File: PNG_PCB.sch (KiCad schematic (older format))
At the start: 1 part, among them U1 Teensy4.1

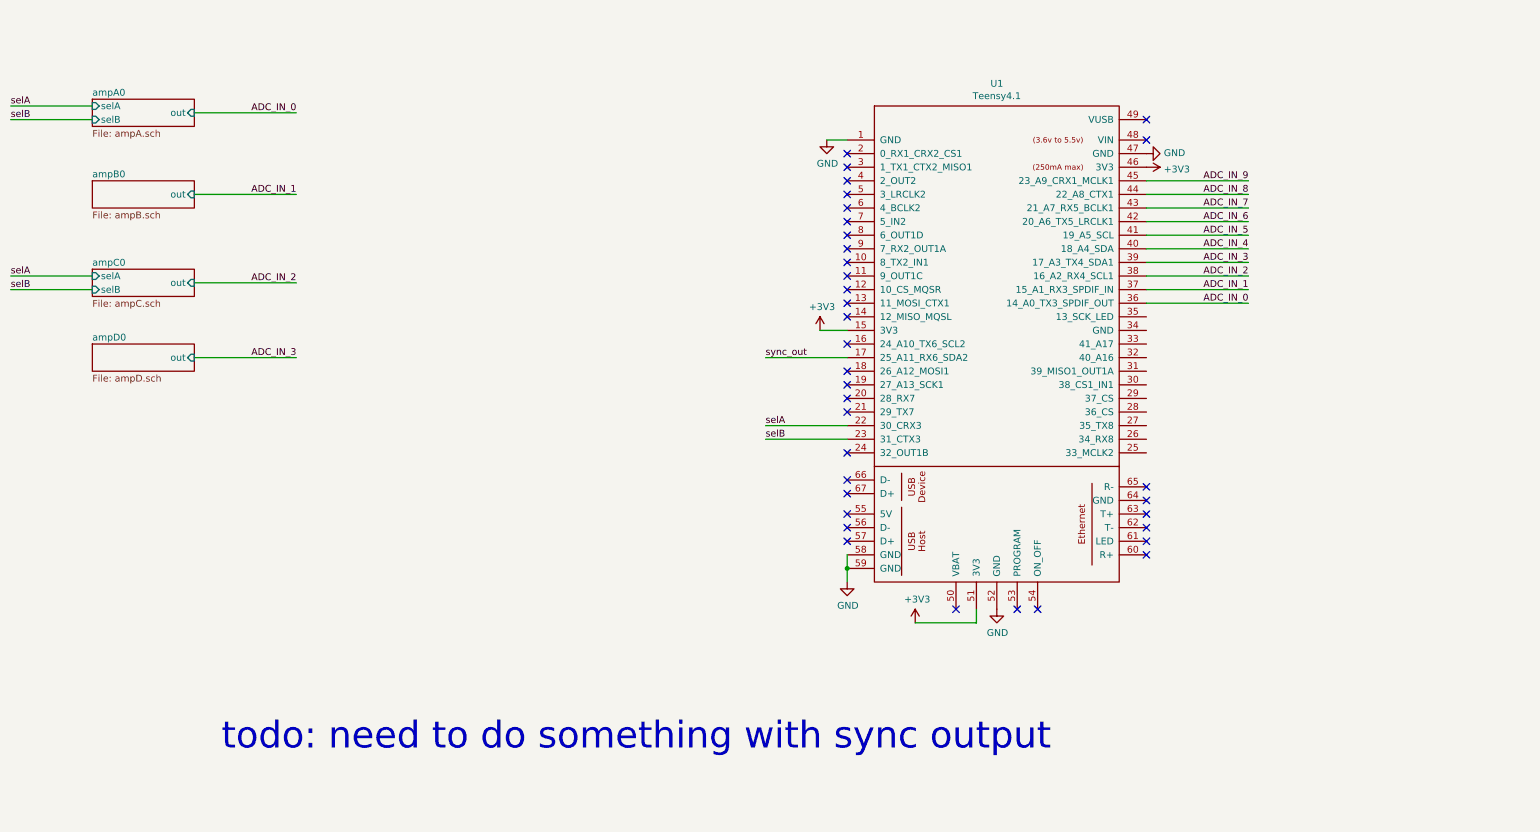
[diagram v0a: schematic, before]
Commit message: added all adc outputs
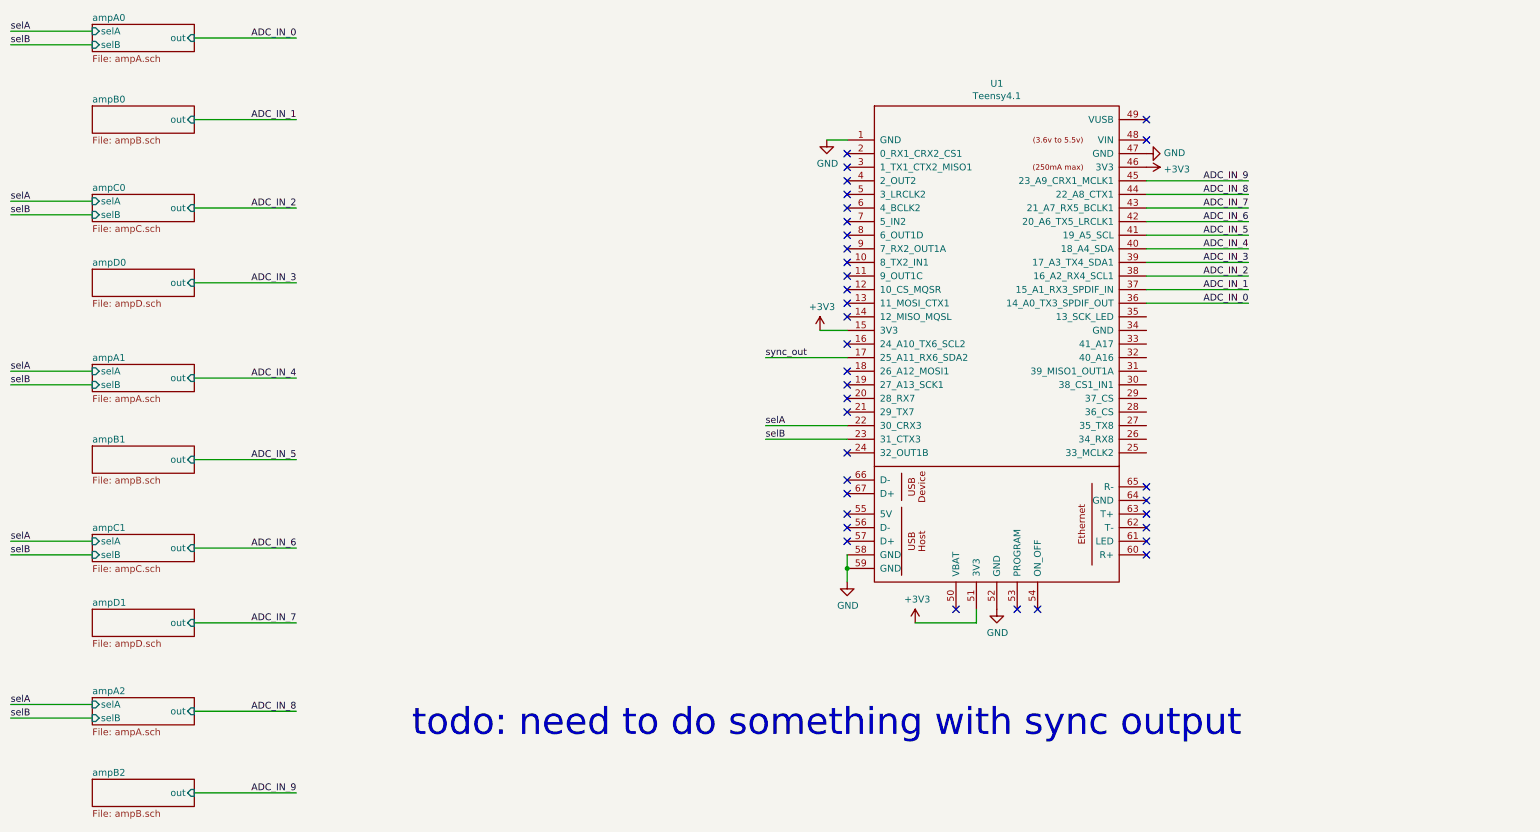
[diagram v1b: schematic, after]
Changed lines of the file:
@@
 $Descr A4 11693 8268
 encoding utf-8
-Sheet 1 5
+Sheet 1 11
 Title ""
 Date ""
@@
 ADC_IN_0
 $Sheet
-S 1750 1350 750  200
+S 1750 800  750  200
 U 6017CC5E
 F0 "ampA0" 50
 F1 "ampA.sch" 50
-F2 "out" I R 2500 1450 50
-F3 "selA" I L 1750 1400 50
-F4 "selB" I L 1750 1500 50
-$EndSheet
-$Sheet
-S 1750 1950 750  200
+F2 "out" I R 2500 900 50
+F3 "selA" I L 1750 850 50
+F4 "selB" I L 1750 950 50
+$EndSheet
+$Sheet
+S 1750 1400 750  200
 U 601927EB
 F0 "ampB0" 50
 F1 "ampB.sch" 50
-F2 "out" I R 2500 2050 50
-$EndSheet
-$Sheet
-S 1750 2600 750  200
+F2 "out" I R 2500 1500 50
+$EndSheet
+$Sheet
+S 1750 2050 750  200
 U 6019C043
 F0 "ampC0" 50
 F1 "ampC.sch" 50
-F2 "out" I R 2500 2700 50
-F3 "selA" I L 1750 2650 50
-F4 "selB" I L 1750 2750 50
-$EndSheet
-$Sheet
-S 1750 3150 750  200
+F2 "out" I R 2500 2150 50
+F3 "selA" I L 1750 2100 50
+F4 "selB" I L 1750 2200 50
+$EndSheet
+$Sheet
+S 1750 2600 750  200
 U 6019DBCE
 F0 "ampD0" 50
 F1 "ampD.sch" 50
-F2 "out" I R 2500 3250 50
-$EndSheet
-$Comp
-L power:GND #PWR?
+F2 "out" I R 2500 2700 50
+$EndSheet
+$Comp
+L power:GND #PWR05
 U 1 1 601A016E
 P 8400 5100
-F 0 "#PWR?" H 8400 4850 50  0001 C CNN
+F 0 "#PWR05" H 8400 4850 50  0001 C CNN
 F 1 "GND" H 8405 4927 50  0000 C CNN
 F 2 "" H 8400 5100 50  0001 C CNN
@@
 $EndComp
 $Comp
-L power:+3V3 #PWR?
+L power:+3V3 #PWR04
 U 1 1 601A19F5
 P 7800 5200
-F 0 "#PWR?" H 7800 5050 50  0001 C CNN
+F 0 "#PWR04" H 7800 5050 50  0001 C CNN
 F 1 "+3V3" H 7815 5373 50  0000 C CNN
 F 2 "" H 7800 5200 50  0001 C CNN
@@
 NoConn ~ 7300 4150
 $Comp
-L power:GND #PWR?
+L power:GND #PWR03
 U 1 1 601A37A3
 P 7300 4900
-F 0 "#PWR?" H 7300 4650 50  0001 C CNN
+F 0 "#PWR03" H 7300 4650 50  0001 C CNN
 F 1 "GND" H 7305 4727 50  0000 C CNN
 F 2 "" H 7300 4900 50  0001 C CNN
@@
 ADC_IN_9
 $Comp
-L power:+3V3 #PWR?
+L power:+3V3 #PWR07
 U 1 1 601A66F3
 P 9500 1850
-F 0 "#PWR?" H 9500 1700 50  0001 C CNN
+F 0 "#PWR07" H 9500 1700 50  0001 C CNN
 F 1 "+3V3" V 9515 1978 50  0000 L CNN
 F 2 "" H 9500 1850 50  0001 C CNN
@@
 $EndComp
 $Comp
-L power:GND #PWR?
+L power:GND #PWR06
 U 1 1 601A740A
 P 9500 1750
-F 0 "#PWR?" H 9500 1500 50  0001 C CNN
+F 0 "#PWR06" H 9500 1500 50  0001 C CNN
 F 1 "GND" V 9505 1622 50  0000 R CNN
 F 2 "" H 9500 1750 50  0001 C CNN
@@
 NoConn ~ 9500 1500
 $Comp
-L power:GND #PWR?
+L power:GND #PWR02
 U 1 1 601A93E9
 P 7150 1650
-F 0 "#PWR?" H 7150 1400 50  0001 C CNN
+F 0 "#PWR02" H 7150 1400 50  0001 C CNN
 F 1 "GND" H 7155 1477 50  0000 C CNN
 F 2 "" H 7150 1650 50  0001 C CNN
@@
 NoConn ~ 7300 3650
 $Comp
-L power:+3V3 #PWR?
+L power:+3V3 #PWR01
 U 1 1 601AD0C3
 P 7100 3050
-F 0 "#PWR?" H 7100 2900 50  0001 C CNN
+F 0 "#PWR01" H 7100 2900 50  0001 C CNN
 F 1 "+3V3" H 7115 3223 50  0000 C CNN
 F 2 "" H 7100 3050 50  0001 C CNN
@@
 Text Label 6700 3250 0    50   ~ 0
 sync_out
-Text Notes 2700 6150 0    197  ~ 0
+Text Notes 4100 6050 0    197  ~ 0
 todo: need to do something with sync output
-Text Label 1150 1400 0    50   ~ 0
-selA
-Text Label 1150 1500 0    50   ~ 0
-selB
-Wire Wire Line
-	1750 1400 1150 1400
-Wire Wire Line
-	1750 1500 1150 1500
-Text Label 1150 2650 0    50   ~ 0
-selA
-Text Label 1150 2750 0    50   ~ 0
-selB
-Wire Wire Line
-	1750 2650 1150 2650
-Wire Wire Line
-	1750 2750 1150 2750
-Wire Wire Line
-	2500 1450 3250 1450
-Text Label 3250 1450 2    50   ~ 0
+Text Label 1150 850  0    50   ~ 0
+selA
+Text Label 1150 950  0    50   ~ 0
+selB
+Wire Wire Line
+	1750 850  1150 850
+Wire Wire Line
+	1750 950  1150 950
+Text Label 1150 2100 0    50   ~ 0
+selA
+Text Label 1150 2200 0    50   ~ 0
+selB
+Wire Wire Line
+	1750 2100 1150 2100
+Wire Wire Line
+	1750 2200 1150 2200
+Wire Wire Line
+	2500 900  3250 900
+Text Label 3250 900  2    50   ~ 0
 ADC_IN_0
 Wire Wire Line
-	2500 2050 3250 2050
-Text Label 3250 2050 2    50   ~ 0
+	2500 1500 3250 1500
+Text Label 3250 1500 2    50   ~ 0
 ADC_IN_1
+Wire Wire Line
+	2500 2150 3250 2150
+Text Label 3250 2150 2    50   ~ 0
+ADC_IN_2
 Wire Wire Line
 	2500 2700 3250 2700
 Text Label 3250 2700 2    50   ~ 0
-ADC_IN_2
-Wire Wire Line
-	2500 3250 3250 3250
-Text Label 3250 3250 2    50   ~ 0
 ADC_IN_3
+$Sheet
+S 1750 3300 750  200
+U 601B4C0E
+F0 "ampA1" 50
+F1 "ampA.sch" 50
+F2 "out" I R 2500 3400 50
+F3 "selA" I L 1750 3350 50
+F4 "selB" I L 1750 3450 50
+$EndSheet
+$Sheet
+S 1750 3900 750  200
+U 601B4C11
+F0 "ampB1" 50
+F1 "ampB.sch" 50
+F2 "out" I R 2500 4000 50
+$EndSheet
+$Sheet
+S 1750 4550 750  200
+U 601B4C16
+F0 "ampC1" 50
+F1 "ampC.sch" 50
+F2 "out" I R 2500 4650 50
+F3 "selA" I L 1750 4600 50
+F4 "selB" I L 1750 4700 50
+$EndSheet
+$Sheet
+S 1750 5100 750  200
+U 601B4C19
+F0 "ampD1" 50
+F1 "ampD.sch" 50
+F2 "out" I R 2500 5200 50
+$EndSheet
+Text Label 1150 3350 0    50   ~ 0
+selA
+Text Label 1150 3450 0    50   ~ 0
+selB
+Wire Wire Line
+	1750 3350 1150 3350
+Wire Wire Line
+	1750 3450 1150 3450
+Text Label 1150 4600 0    50   ~ 0
+selA
+Text Label 1150 4700 0    50   ~ 0
+selB
+Wire Wire Line
+	1750 4600 1150 4600
+Wire Wire Line
+	1750 4700 1150 4700
+Wire Wire Line
+	2500 3400 3250 3400
+Text Label 3250 3400 2    50   ~ 0
+ADC_IN_4
+Wire Wire Line
+	2500 4000 3250 4000
+Text Label 3250 4000 2    50   ~ 0
+ADC_IN_5
+Wire Wire Line
+	2500 4650 3250 4650
+Text Label 3250 4650 2    50   ~ 0
+ADC_IN_6
+Wire Wire Line
+	2500 5200 3250 5200
+Text Label 3250 5200 2    50   ~ 0
+ADC_IN_7
+$Sheet
+S 1750 5750 750  200
+U 601B73B7
+F0 "ampA2" 50
+F1 "ampA.sch" 50
+F2 "out" I R 2500 5850 50
+F3 "selA" I L 1750 5800 50
+F4 "selB" I L 1750 5900 50
+$EndSheet
+$Sheet
+S 1750 6350 750  200
+U 601B73BA
+F0 "ampB2" 50
+F1 "ampB.sch" 50
+F2 "out" I R 2500 6450 50
+$EndSheet
+Text Label 1150 5800 0    50   ~ 0
+selA
+Text Label 1150 5900 0    50   ~ 0
+selB
+Wire Wire Line
+	1750 5800 1150 5800
+Wire Wire Line
+	1750 5900 1150 5900
+Wire Wire Line
+	2500 5850 3250 5850
+Text Label 3250 5850 2    50   ~ 0
+ADC_IN_8
+Wire Wire Line
+	2500 6450 3250 6450
+Text Label 3250 6450 2    50   ~ 0
+ADC_IN_9
 $EndSCHEMATC

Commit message: added screw terminal port for sync output
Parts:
- added U?: screw_term, Connector_PinHeader_1.27mm:PinHeader_1x02_P1.27mm_Vertical, symbol PNG_PCB_Parts:screw_term
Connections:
- net sync_out: now also U?.1 (a)
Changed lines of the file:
@@
 Text Label 3250 6450 2    50   ~ 0
 ADC_IN_9
+Wire Wire Line
+	5000 3250 4400 3250
+Text Label 4400 3250 0    50   ~ 0
+sync_out
+$Comp
+L PNG_PCB_Parts:screw_term U?
+U 1 1 601BAD2F
+P 5000 3250
+F 0 "U?" H 5058 3384 50  0000 L CNN
+F 1 "screw_term" H 5058 3293 50  0000 L CNN
+F 2 "Connector_PinHeader_1.27mm:PinHeader_1x02_P1.27mm_Vertical" H 5000 3250 50  0001 C CNN
+F 3 "" H 5000 3250 50  0001 C CNN
+	1    5000 3250
+	1    0    0    -1
+$EndComp
 $EndSCHEMATC

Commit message: fixed sync output and added sync input
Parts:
- added U?: screw_term, Connector_PinHeader_1.27mm:PinHeader_1x02_P1.27mm_Vertical, symbol PNG_PCB_Parts:screw_term
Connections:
- net sync_out: now also U1.2 (0_RX1_CRX2_CS1), U?.2 (b); no longer U1.17 (25_A11_RX6_SDA2), U?.1 (a)
- new net sync_in: U1.17 (25_A11_RX6_SDA2), U?.1 (a)
- no-connect marks 35 -> 34
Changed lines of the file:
@@
 L power:GND #PWR02
 U 1 1 601A93E9
-P 7150 1650
-F 0 "#PWR02" H 7150 1400 50  0001 C CNN
-F 1 "GND" H 7155 1477 50  0000 C CNN
-F 2 "" H 7150 1650 50  0001 C CNN
-F 3 "" H 7150 1650 50  0001 C CNN
-	1    7150 1650
-	1    0    0    -1
-$EndComp
-Wire Wire Line
-	7300 1650 7150 1650
-NoConn ~ 7300 1750
+P 7300 1650
+F 0 "#PWR02" H 7300 1400 50  0001 C CNN
+F 1 "GND" V 7305 1522 50  0000 R CNN
+F 2 "" H 7300 1650 50  0001 C CNN
+F 3 "" H 7300 1650 50  0001 C CNN
+	1    7300 1650
+	0    1    1    0
+$EndComp
 NoConn ~ 7300 1850
 NoConn ~ 7300 1950
@@
 	7300 3250 6700 3250
 Text Label 6700 3250 0    50   ~ 0
-sync_out
+sync_in
 Text Notes 4100 6050 0    197  ~ 0
 todo: need to do something with sync output
@@
 	5000 3250 4400 3250
 Text Label 4400 3250 0    50   ~ 0
-sync_out
+sync_in
 $Comp
 L PNG_PCB_Parts:screw_term U?
@@
 	1    0    0    -1
 $EndComp
+Wire Wire Line
+	7300 1750 6700 1750
+Text Label 6700 1750 0    50   ~ 0
+sync_out
+Wire Wire Line
+	5000 3600 4400 3600
+Text Label 4400 3600 0    50   ~ 0
+sync_out
+$Comp
+L PNG_PCB_Parts:screw_term U?
+U 2 1 601BD94C
+P 5000 3600
+F 0 "U?" H 5058 3734 50  0000 L CNN
+F 1 "screw_term" H 5058 3643 50  0000 L CNN
+F 2 "Connector_PinHeader_1.27mm:PinHeader_1x02_P1.27mm_Vertical" H 5000 3600 50  0001 C CNN
+F 3 "" H 5000 3600 50  0001 C CNN
+	2    5000 3600
+	1    0    0    -1
+$EndComp

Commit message: annotated sync in and out
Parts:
- gave numbers to parts that had none: 1
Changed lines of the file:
@@
 sync_in
 $Comp
-L PNG_PCB_Parts:screw_term U?
+L PNG_PCB_Parts:screw_term U31
 U 1 1 601BAD2F
 P 5000 3250
-F 0 "U?" H 5058 3384 50  0000 L CNN
+F 0 "U31" H 5058 3384 50  0000 L CNN
 F 1 "screw_term" H 5058 3293 50  0000 L CNN
 F 2 "Connector_PinHeader_1.27mm:PinHeader_1x02_P1.27mm_Vertical" H 5000 3250 50  0001 C CNN
@@
 sync_out
 $Comp
-L PNG_PCB_Parts:screw_term U?
+L PNG_PCB_Parts:screw_term U31
 U 2 1 601BD94C
 P 5000 3600
-F 0 "U?" H 5058 3734 50  0000 L CNN
+F 0 "U31" H 5058 3734 50  0000 L CNN
 F 1 "screw_term" H 5058 3643 50  0000 L CNN
 F 2 "Connector_PinHeader_1.27mm:PinHeader_1x02_P1.27mm_Vertical" H 5000 3600 50  0001 C CNN

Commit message: added no connects on teensy
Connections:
- no-connect marks 34 -> 45
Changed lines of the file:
@@
 	1    0    0    -1
 $EndComp
+NoConn ~ 9500 2950
+NoConn ~ 9500 3050
+NoConn ~ 9500 3150
+NoConn ~ 9500 3250
+NoConn ~ 9500 3350
+NoConn ~ 9500 3450
+NoConn ~ 9500 3550
+NoConn ~ 9500 3650
+NoConn ~ 9500 3750
+NoConn ~ 9500 3850
+NoConn ~ 9500 3950
 $EndSCHEMATC

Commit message: added all muxes to the board
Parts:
- renumbered U31 to U1, U1 to U2
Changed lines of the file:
@@
 $EndDescr
 $Comp
-L teensy:Teensy4.1 U1
+L teensy:Teensy4.1 U2
 U 1 1 60133249
 P 8400 3800
-F 0 "U1" H 8400 6365 50  0000 C CNN
+F 0 "U2" H 8400 6365 50  0000 C CNN
 F 1 "Teensy4.1" H 8400 6274 50  0000 C CNN
 F 2 "teensy:Teensy41" H 8000 4200 50  0001 C CNN
@@
 sync_in
 $Comp
-L PNG_PCB_Parts:screw_term U31
+L PNG_PCB_Parts:screw_term U1
 U 1 1 601BAD2F
 P 5000 3250
-F 0 "U31" H 5058 3384 50  0000 L CNN
+F 0 "U1" H 5058 3384 50  0000 L CNN
 F 1 "screw_term" H 5058 3293 50  0000 L CNN
 F 2 "Connector_PinHeader_1.27mm:PinHeader_1x02_P1.27mm_Vertical" H 5000 3250 50  0001 C CNN
@@
 sync_out
 $Comp
-L PNG_PCB_Parts:screw_term U31
+L PNG_PCB_Parts:screw_term U1
 U 2 1 601BD94C
 P 5000 3600
-F 0 "U31" H 5058 3734 50  0000 L CNN
+F 0 "U1" H 5058 3734 50  0000 L CNN
 F 1 "screw_term" H 5058 3643 50  0000 L CNN
 F 2 "Connector_PinHeader_1.27mm:PinHeader_1x02_P1.27mm_Vertical" H 5000 3600 50  0001 C CNN

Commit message: removed todo note
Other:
- note removed: "todo: need to do something with sync output"
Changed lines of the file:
@@
 Text Label 6700 3250 0    50   ~ 0
 sync_in
-Text Notes 4100 6050 0    197  ~ 0
-todo: need to do something with sync output
 Text Label 1150 850  0    50   ~ 0
 selA
